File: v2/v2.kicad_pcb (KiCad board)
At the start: 2 copper layers, 95.2 x 95.2 mm, 65 parts, among them J1 rBUSoutV, J10 mcuTIEout, J2 rBUSinV, J3 cTIEoutV, J4 cTIEinV, J5 cBUSoutH, J6 cTIEoutH, J7 mcuTIEin, J8 cTIEinH, J9 cBUSinH, SW1 KeySwitch, SW10 KeySwitch, SW11 KeySwitch, SW12 KeySwitch, SW13 KeySwitch, SW14 KeySwitch, SW15 KeySwitch, SW16 KeySwitch, SW17 KeySwitch, SW18 KeySwitch, SW19 KeySwitch, SW2 KeySwitch, SW20 KeySwitch, SW21 KeySwitch, SW22 KeySwitch, SW23 KeySwitch, SW24 KeySwitch, SW25 KeySwitch, SW3 KeySwitch, SW4 KeySwitch, SW5 KeySwitch, SW6 KeySwitch, SW7 KeySwitch, SW8 KeySwitch, SW9 KeySwitch, U1 ItsyBitsy5V

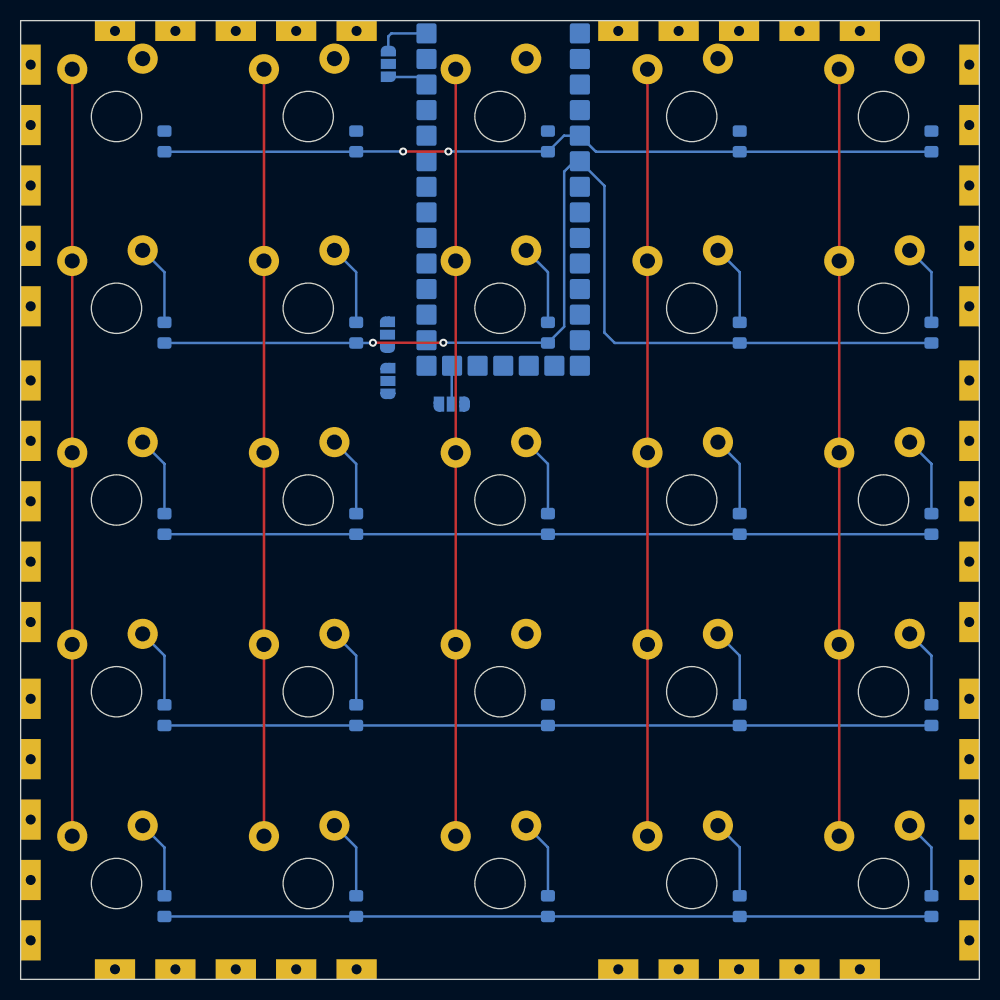
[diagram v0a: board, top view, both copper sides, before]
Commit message: Finish v2 keyboard tile
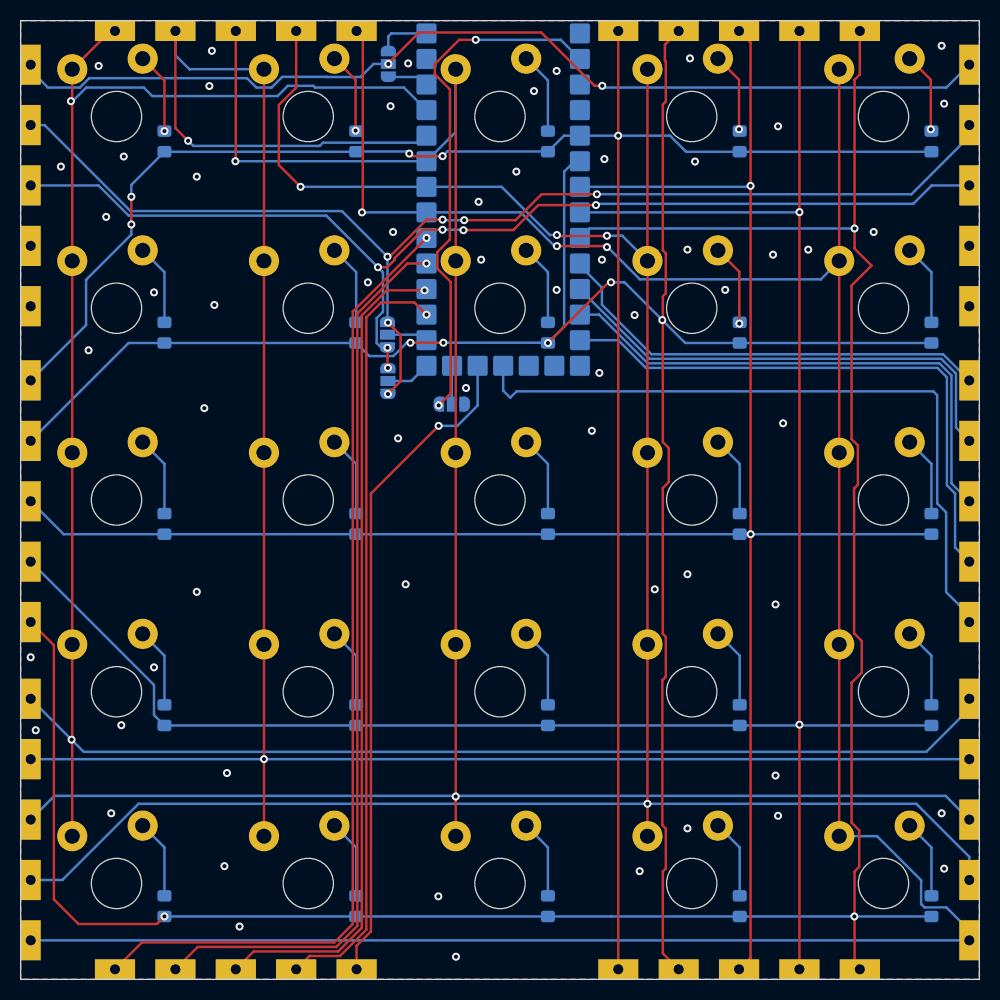
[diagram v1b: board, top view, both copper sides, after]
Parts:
- JP1, JP2, JP3, JP4: footprint ProjectLibrary:SolderJumper-3_P1.3mm_Open_RoundedPad1.0x1.5mm_No_Silk -> Jumper:SolderJumper-3_P1.3mm_Open_RoundedPad1.0x1.5mm
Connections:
- J10 pad 2: /mRXsTX -> /mTXsRX
- J10 pad 3: /mTXsRX -> /mRXsTX
- J3 pad 1: /b0c2 -> /b0c1
- J4 pad 1: /b0c2 -> /b0c1
- J7 pad 2: /mRXsTX -> /mTXsRX
- J7 pad 3: /mTXsRX -> /mRXsTX
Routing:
- net /b0r5: track 76.2 -> 257.9 mm, vias 0 -> 3
- net /b0c5: track 76.2 -> 241.5 mm, vias 0 -> 3
- net /b0r4: track 76.2 -> 231.7 mm, vias 0 -> 4
- net /b0r1: track 76.2 -> 218.5 mm, vias 0 -> 2
- net /b0r2: track 76.2 -> 217.0 mm, vias 0 -> 2
- net /b0r3: track 76.2 -> 214.3 mm, vias 0 -> 2
- net /b0c4: track 76.2 -> 213.0 mm, vias 0 -> 2
- net /b0c3: track 76.2 -> 202.0 mm, vias 0 -> 2
- net /b0c1: track 77.5 -> 199.5 mm, vias 2 -> 5
- net /mTXsRX: track 0.00 -> 119.5 mm, vias 0 -> 6
- net /mRXsTX: track 0.00 -> 111.4 mm, vias 0 -> 6
- net /b0c2: track 108.8 -> 215.2 mm, vias 2 -> 5
- net +VDC: track 0.00 -> 100.8 mm, vias 0 -> 2
- net /b1r1: track 0.00 -> 96.7 mm, vias 0 -> 1
- net /b1r2: track 0.00 -> 89.6 mm, vias 0 -> 1
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- added copper zone on B.Cu, net GND
- added copper zone on F.Cu, net GND

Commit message: Change diode to SOD-123, some tweaks
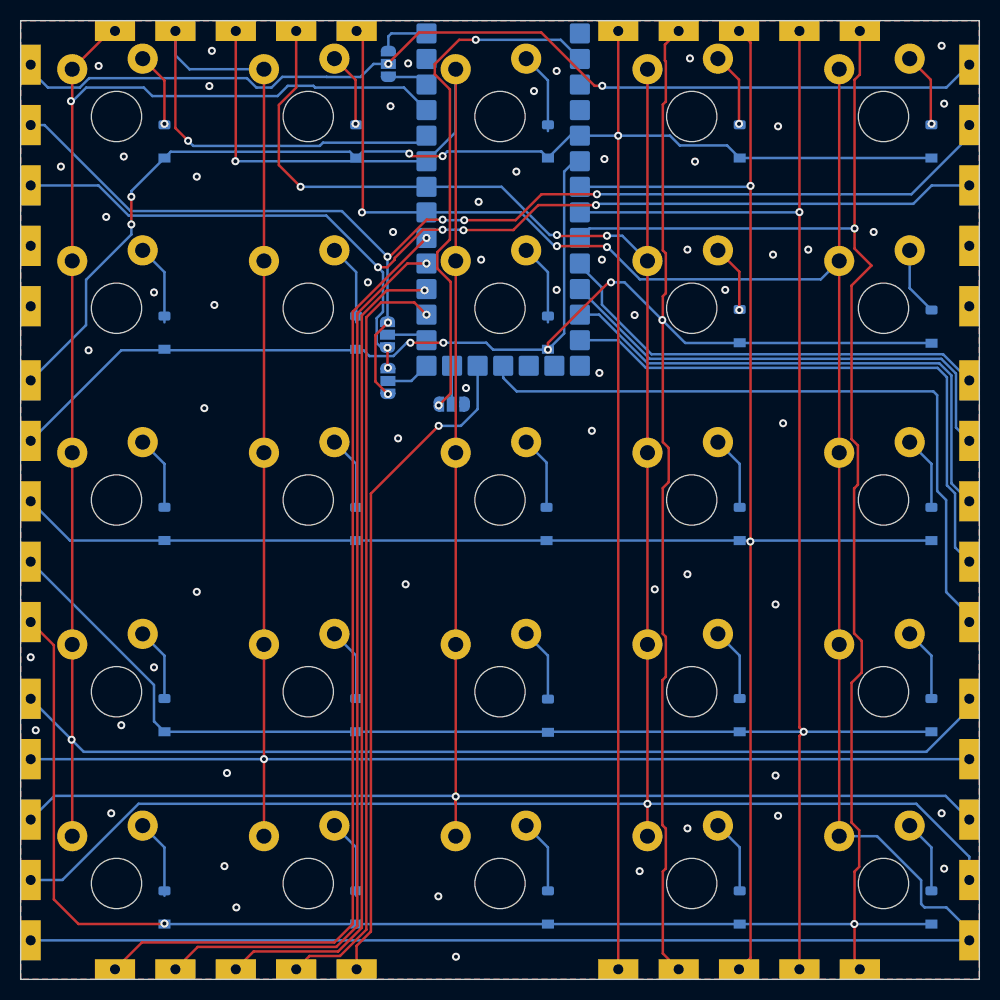
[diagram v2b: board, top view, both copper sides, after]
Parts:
- D1, D10, D11, D12, D13, D14, D15, D16, D17, D18, D19, D2, D20, D21, D22, D23, D24, D25, D3, D4, D5, D6, D7, D8, D9: footprint ProjectLibrary:D_0805_2012Metric_Pad1.15x1.40mm_HandSolder_No_Silk -> ProjectLibrary:D_SOD-123_NoSilk
- moved D9 0.65 mm to (119.1, 78.0)
- moved D10 0.60 mm to (138.1, 78.0)
- moved D13 0.14 mm to (99.9, 97.6)
- moved D21 0.13 mm to (61.9, 135.7)
- moved D22 0.13 mm to (81.0, 135.7)
- moved D23 0.13 mm to (100.0, 135.7)
- moved D24 0.13 mm to (119.1, 135.7)
- moved D25 0.13 mm to (138.1, 135.7)
- moved D18 0.06 mm to (100.0, 116.7)
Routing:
- net Net-(D9-Pad1): track 8.30 -> 6.81 mm
- net /b1c5: track 70.2 -> 68.9 mm
- net Net-(D10-Pad1): track 8.05 -> 6.84 mm
- net /b0c2: track 215.2 -> 216.2 mm
- net /b0c4: track 213.0 -> 214.0 mm
- net /b0c1: track 199.5 -> 200.3 mm
- net Net-(D2-Pad1): track 8.10 -> 7.34 mm
- net Net-(D1-Pad1): track 8.10 -> 7.37 mm
- net Net-(D13-Pad1): track 8.00 -> 7.32 mm
- net Net-(D4-Pad1): track 8.10 -> 7.43 mm
- net Net-(D20-Pad1): track 7.95 -> 7.32 mm
- net Net-(D19-Pad1): track 7.95 -> 7.32 mm
- net Net-(D17-Pad1): track 7.95 -> 7.32 mm
- net Net-(D16-Pad1): track 7.95 -> 7.32 mm
- net Net-(D11-Pad1): track 8.00 -> 7.37 mm
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
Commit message: Fix key order & run DRC
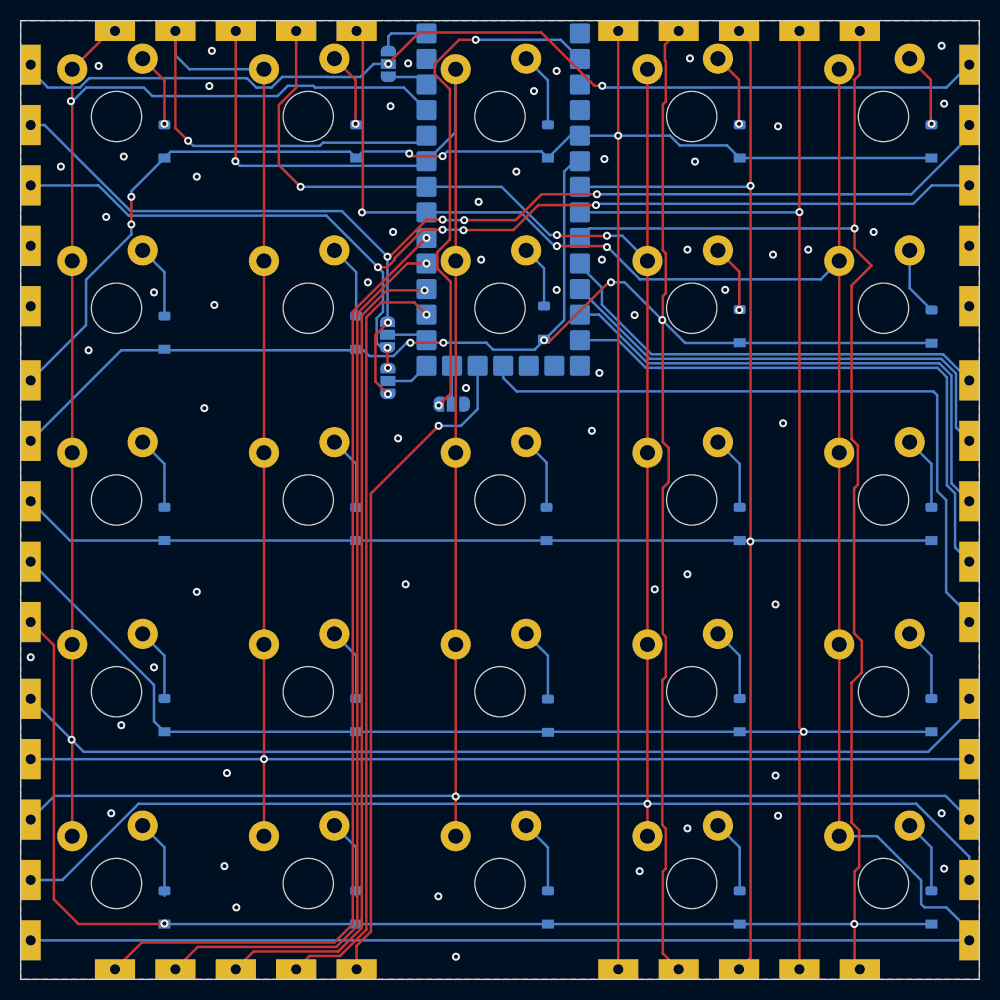
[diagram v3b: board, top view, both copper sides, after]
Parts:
- J1: value rBUSoutV -> cBUSoutV
- J2: value rBUSinV -> cBUSinV
- J5: value cBUSoutH -> rBUSoutH
- J9: value cBUSinH -> rBUSinH
- moved D8 1.07 mm to (99.6, 77.6)
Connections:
- D1 pad 2: /b0c1 -> /b0r1
- D10 pad 2: /b0c2 -> /b0r2
- D11 pad 2: /b0c3 -> /b0r3
- D12 pad 2: /b0c3 -> /b0r3
- D13 pad 2: /b0c3 -> /b0r3
- D14 pad 2: /b0c3 -> /b0r3
- D15 pad 2: /b0c3 -> /b0r3
- D16 pad 2: /b0c4 -> /b0r4
- D17 pad 2: /b0c4 -> /b0r4
- D18 pad 2: /b0c4 -> /b0r4
- D19 pad 2: /b0c4 -> /b0r4
- D2 pad 2: /b0c1 -> /b0r1
- D20 pad 2: /b0c4 -> /b0r4
- D21 pad 2: /b0c5 -> /b0r5
- D22 pad 2: /b0c5 -> /b0r5
- D23 pad 2: /b0c5 -> /b0r5
- D24 pad 2: /b0c5 -> /b0r5
- D25 pad 2: /b0c5 -> /b0r5
- D3 pad 2: /b0c1 -> /b0r1
- D4 pad 2: /b0c1 -> /b0r1
- D5 pad 2: /b0c1 -> /b0r1
- D6 pad 2: /b0c2 -> /b0r2
- D7 pad 2: /b0c2 -> /b0r2
- D8 pad 2: /b0c2 -> /b0r2
- D9 pad 2: /b0c2 -> /b0r2
- J1 pad 1: /b0r1 -> /b0c1
- J1 pad 2: /b0r2 -> /b0c2
- J1 pad 3: /b0r3 -> /b0c3
- J1 pad 4: /b0r4 -> /b0c4
- J1 pad 5: /b0r5 -> /b0c5
- J2 pad 1: /b1r1 -> /b1c1
- J2 pad 2: /b1r2 -> /b1c2
- J2 pad 3: /b1r3 -> /b1c3
- J2 pad 4: /b1r4 -> /b1c4
- J2 pad 5: /b1r5 -> /b1c5
- J3 pad 1: /b0c1 -> /b0r1
- J3 pad 2: /b0c2 -> /b0r2
- J3 pad 3: /b0c3 -> /b0r3
- J3 pad 4: /b0c4 -> /b0r4
- J3 pad 5: /b0c5 -> /b0r5
- J4 pad 1: /b0c1 -> /b0r1
- J4 pad 2: /b0c2 -> /b0r2
- J4 pad 3: /b0c3 -> /b0r3
- J4 pad 4: /b0c4 -> /b0r4
- J4 pad 5: /b0c5 -> /b0r5
- J5 pad 1: /b0c1 -> /b0r1
- J5 pad 2: /b0c2 -> /b0r2
- J5 pad 3: /b0c3 -> /b0r3
- J5 pad 4: /b0c4 -> /b0r4
- J5 pad 5: /b0c5 -> /b0r5
- J6 pad 1: /b0r1 -> /b0c1
- J6 pad 2: /b0r2 -> /b0c2
- J6 pad 3: /b0r3 -> /b0c3
- J6 pad 4: /b0r4 -> /b0c4
- J6 pad 5: /b0r5 -> /b0c5
- J8 pad 1: /b0r1 -> /b0c1
- J8 pad 2: /b0r2 -> /b0c2
- J8 pad 3: /b0r3 -> /b0c3
- J8 pad 4: /b0r4 -> /b0c4
- J8 pad 5: /b0r5 -> /b0c5
- J9 pad 1: /b1c1 -> /b1r1
- J9 pad 2: /b1c2 -> /b1r2
- J9 pad 3: /b1c3 -> /b1r3
- J9 pad 4: /b1c4 -> /b1r4
- J9 pad 5: /b1c5 -> /b1r5
- SW1 pad 1: /b0r1 -> /b0c1
- SW10 pad 1: /b0r5 -> /b0c5
- SW11 pad 1: /b0r1 -> /b0c1
- SW12 pad 1: /b0r2 -> /b0c2
- SW13 pad 1: /b0r3 -> /b0c3
- SW14 pad 1: /b0r4 -> /b0c4
- SW15 pad 1: /b0r5 -> /b0c5
- SW16 pad 1: /b0r1 -> /b0c1
- SW17 pad 1: /b0r2 -> /b0c2
- SW18 pad 1: /b0r3 -> /b0c3
- SW19 pad 1: /b0r4 -> /b0c4
- SW2 pad 1: /b0r2 -> /b0c2
- SW20 pad 1: /b0r5 -> /b0c5
- SW21 pad 1: /b0r1 -> /b0c1
- SW22 pad 1: /b0r2 -> /b0c2
- SW23 pad 1: /b0r3 -> /b0c3
- SW24 pad 1: /b0r4 -> /b0c4
- SW25 pad 1: /b0r5 -> /b0c5
- SW3 pad 1: /b0r3 -> /b0c3
- SW4 pad 1: /b0r4 -> /b0c4
- SW5 pad 1: /b0r5 -> /b0c5
- SW6 pad 1: /b0r1 -> /b0c1
- SW7 pad 1: /b0r2 -> /b0c2
- SW8 pad 1: /b0r3 -> /b0c3
- SW9 pad 1: /b0r4 -> /b0c4
- U1 pad 10: /b1c1 -> /b1r1
- U1 pad 11: /b1c2 -> /b1r2
- U1 pad 12: /b1c3 -> /b1r3
- U1 pad 13: /b1c4 -> /b1r4
- U1 pad 17: /b1c5 -> /b1r5
- U1 pad 18: /b1r5 -> /b1c5
- U1 pad 22: /b1r4 -> /b1c4
- U1 pad 23: /b1r3 -> /b1c3
- U1 pad 24: /b1r2 -> /b1c2
- U1 pad 25: /b1r1 -> /b1c1
- U1 pad 26: /b0r5 -> /b0c5
- U1 pad 27: /b0r4 -> /b0c4
- U1 pad 28: /b0r3 -> /b0c3
- U1 pad 29: /b0r2 -> /b0c2
- U1 pad 30: /b0r1 -> /b0c1
- U1 pad 5: /b0c1 -> /b0r1
- U1 pad 6: /b0c2 -> /b0r2
- U1 pad 7: /b0c3 -> /b0r3
- U1 pad 8: /b0c4 -> /b0r4
- U1 pad 9: /b0c5 -> /b0r5
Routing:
- net /b1r1: track 96.7 -> 44.4 mm, vias 1 -> 0
- net /b1c1: track 44.6 -> 96.7 mm, vias 0 -> 1
- net /b1r2: track 89.6 -> 48.1 mm, vias 1 -> 0
- net /b1c2: track 48.1 -> 89.6 mm, vias 0 -> 1
- net /b1r3: track 82.3 -> 52.7 mm, vias 1 -> 0
- net /b1c3: track 52.7 -> 82.3 mm, vias 0 -> 1
- net /b1r4: track 76.5 -> 57.2 mm, vias 1 -> 0
- net /b1c4: track 57.2 -> 76.5 mm, vias 0 -> 1
- net /b0r1: track 218.5 -> 199.9 mm, vias 2 -> 5
- net /b0r4: track 231.7 -> 214.0 mm, vias 4 -> 2
- net /b0c4: track 214.0 -> 231.7 mm, vias 2 -> 4
- net /b0r5: track 257.9 -> 240.5 mm
- net /b0c1: track 200.3 -> 216.6 mm, vias 5 -> 2
- net /b0c5: track 241.3 -> 256.0 mm
- net /b0r3: track 214.3 -> 202.3 mm
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
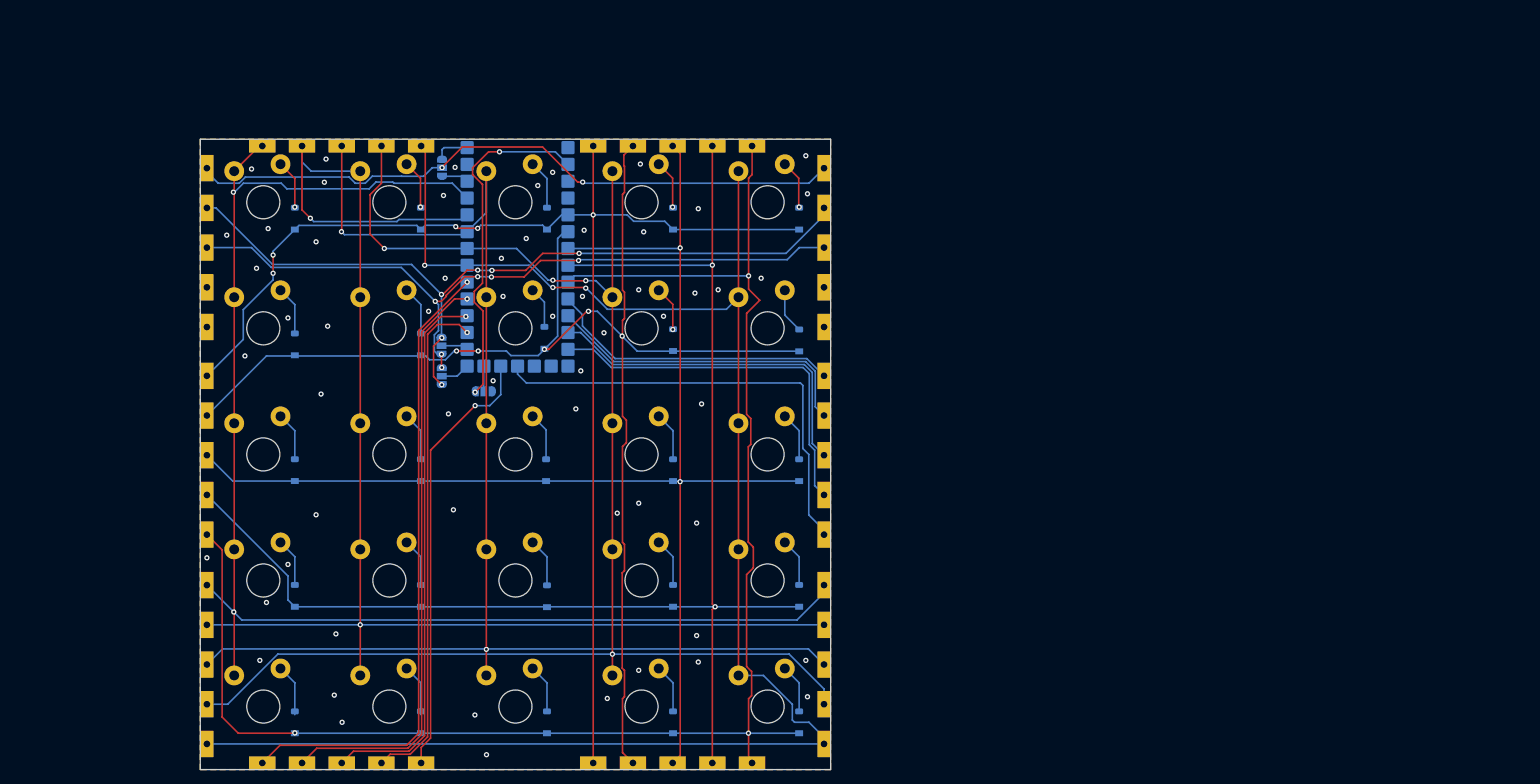
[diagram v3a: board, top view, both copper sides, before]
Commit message: Refactor to include USB
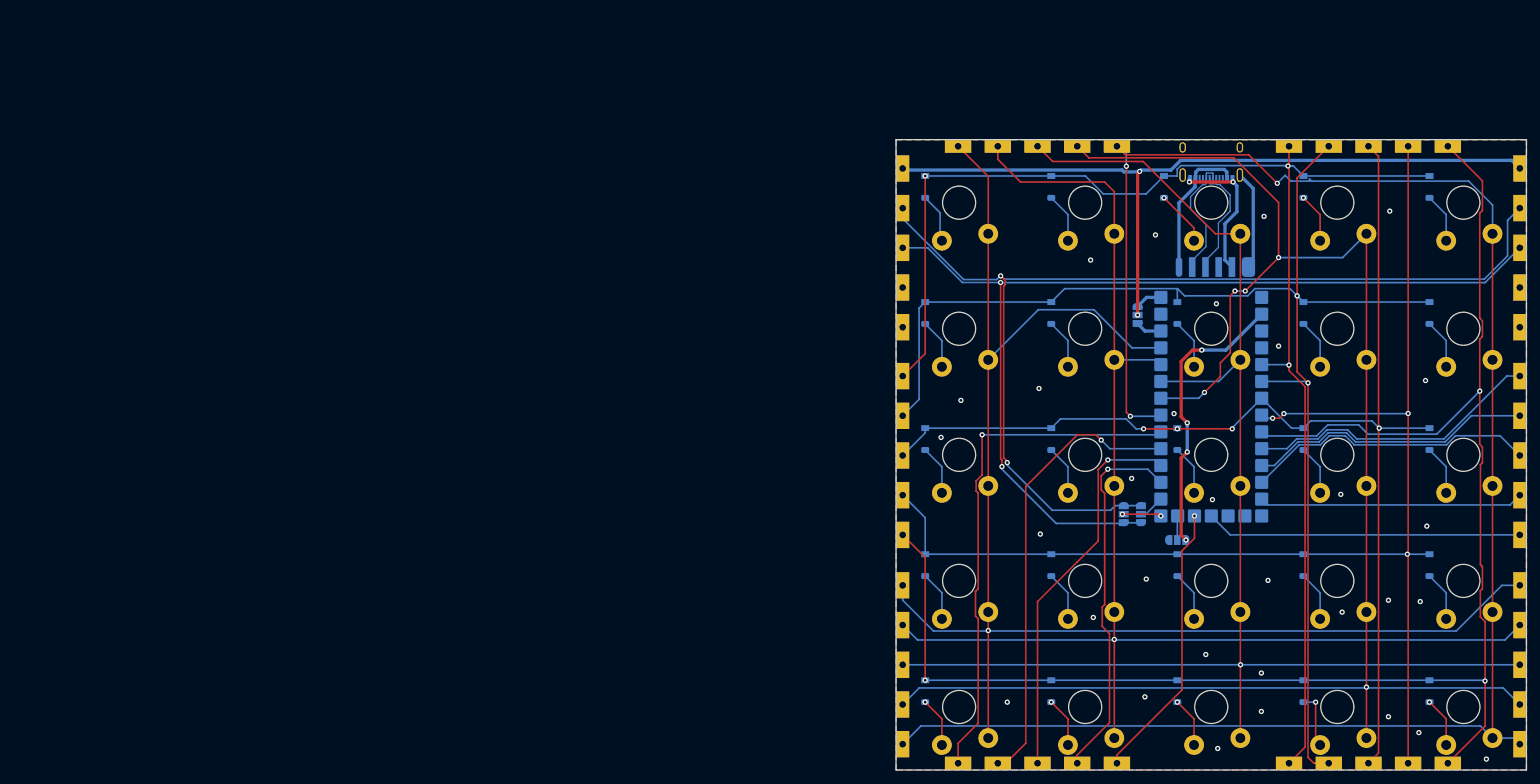
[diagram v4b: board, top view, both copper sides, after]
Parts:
- added J11: USB_C_Receptacle_USB2.0, ProjectLibrary:USB_C_Receptacle_XKB_U262-16XN-4BVC11_NoSilk, B.Cu at (200.4, 49.9)
- added J12: Conn_01x06_Female, ProjectLibrary:USB_JUMP_PAD, B.Cu at (207.0, 65.4)
- JP1, JP2, JP3, JP4: footprint Jumper:SolderJumper-3_P1.3mm_Open_RoundedPad1.0x1.5mm -> ProjectLibrary:SolderJumper-3_P1.3mm_Open_RoundedPad1.0x1.5mm_No_Silk
- moved JP3 108.7 mm to (189.8, 104.3)
- moved JP2 107.4 mm to (189.3, 74.2)
- moved U1 107.2 mm to (209.3, 70.3)
- moved JP1 107.2 mm to (195.3, 108.2), turned to 180 degrees
- moved JP4 105.1 mm to (187.2, 104.3), turned to 90 degrees
- moved SW10 105.1 mm to (238.5, 76.3), turned to 180 degrees
- moved SW15 105.1 mm to (238.5, 95.3), turned to 180 degrees
- moved SW20 105.1 mm to (238.5, 114.4), turned to 180 degrees
- moved SW25 105.1 mm to (238.5, 133.4), turned to 180 degrees
- moved SW5 105.1 mm to (238.5, 57.2), turned to 180 degrees
- moved SW12 105.1 mm to (181.3, 95.3), turned to 180 degrees
- moved SW14 105.1 mm to (219.4, 95.3), turned to 180 degrees
- moved SW17 105.1 mm to (181.3, 114.4), turned to 180 degrees
- moved SW19 105.1 mm to (219.4, 114.4), turned to 180 degrees
- moved SW2 105.1 mm to (181.3, 57.2), turned to 180 degrees
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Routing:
- net /mTXsRX: track 118.2 -> 159.2 mm, vias 6 -> 2
- net /mRXsTX: track 110.8 -> 150.3 mm, vias 6 -> 2
- net /b0c4: track 231.7 -> 261.4 mm, vias 4 -> 5
- net /b0c5: track 256.0 -> 285.1 mm
- net /b1c5: track 66.2 -> 42.2 mm
- net /b1c3: track 82.3 -> 58.6 mm
- net /USB_GND: track 0.00 -> 21.8 mm, vias 0 -> 2
- net /USB_VCC: track 0.00 -> 21.4 mm
- net /b1c2: track 89.6 -> 68.8 mm
- net /b1r5: track 68.2 -> 47.8 mm
- net /b0r3: track 202.3 -> 182.2 mm, vias 2 -> 4
- net /b1c4: track 76.5 -> 56.5 mm
- net /USB_D-: track 0.00 -> 19.0 mm
- net /b1c1: track 96.7 -> 78.9 mm
- net /USB_D+: track 0.00 -> 17.7 mm
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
